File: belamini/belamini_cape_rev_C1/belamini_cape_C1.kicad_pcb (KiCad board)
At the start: 4 copper layers, 55 x 35 mm, 60 parts, among them IC1 TSV524xIQ4T, IC2 TSV524xIQ4T, IC3 ADS8168, IC4 TLV320AIC3104, IC5 MIC5317, IC6 USBLC6-2SC6, J1 Conn_01x10, J2 Conn_01x03, J3 Conn_01x03, J4 Conn_01x03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

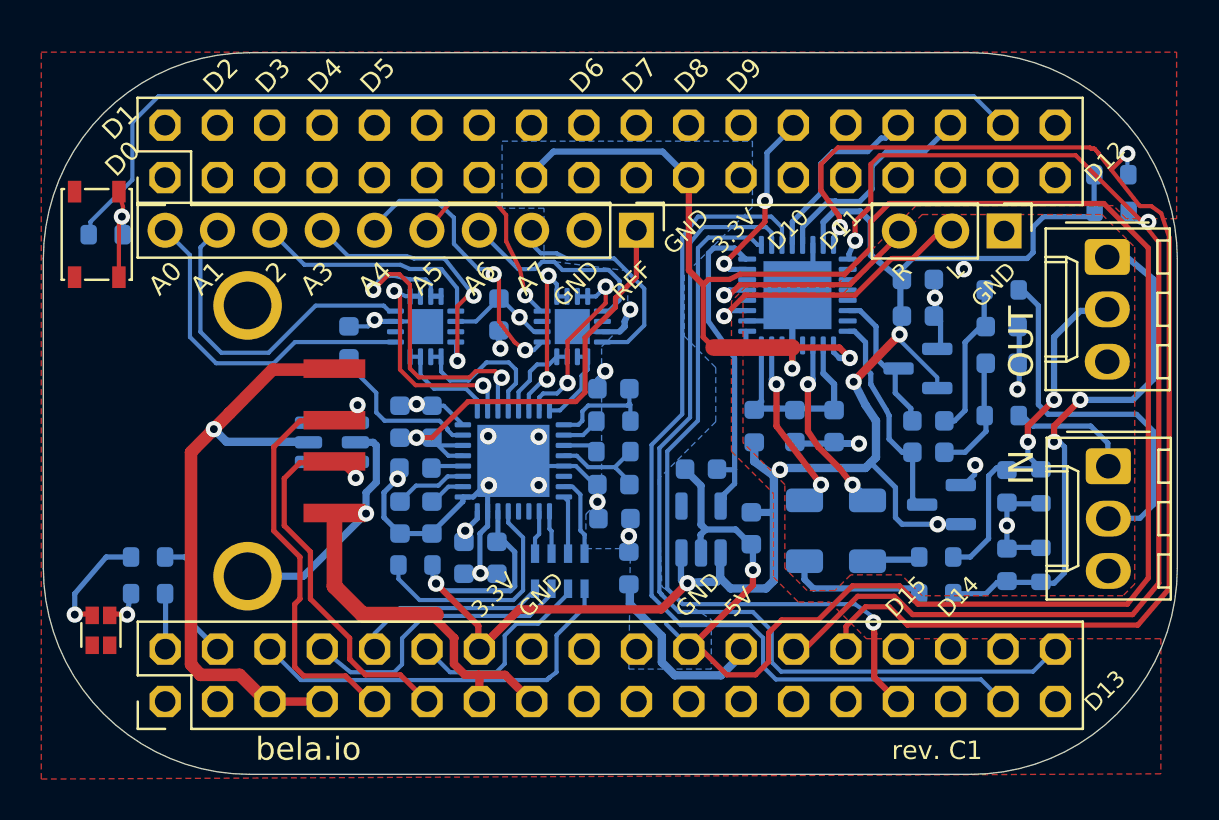
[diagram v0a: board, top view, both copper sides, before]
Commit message: Add logo to Mini rev. C1, clean up schematic and add production files
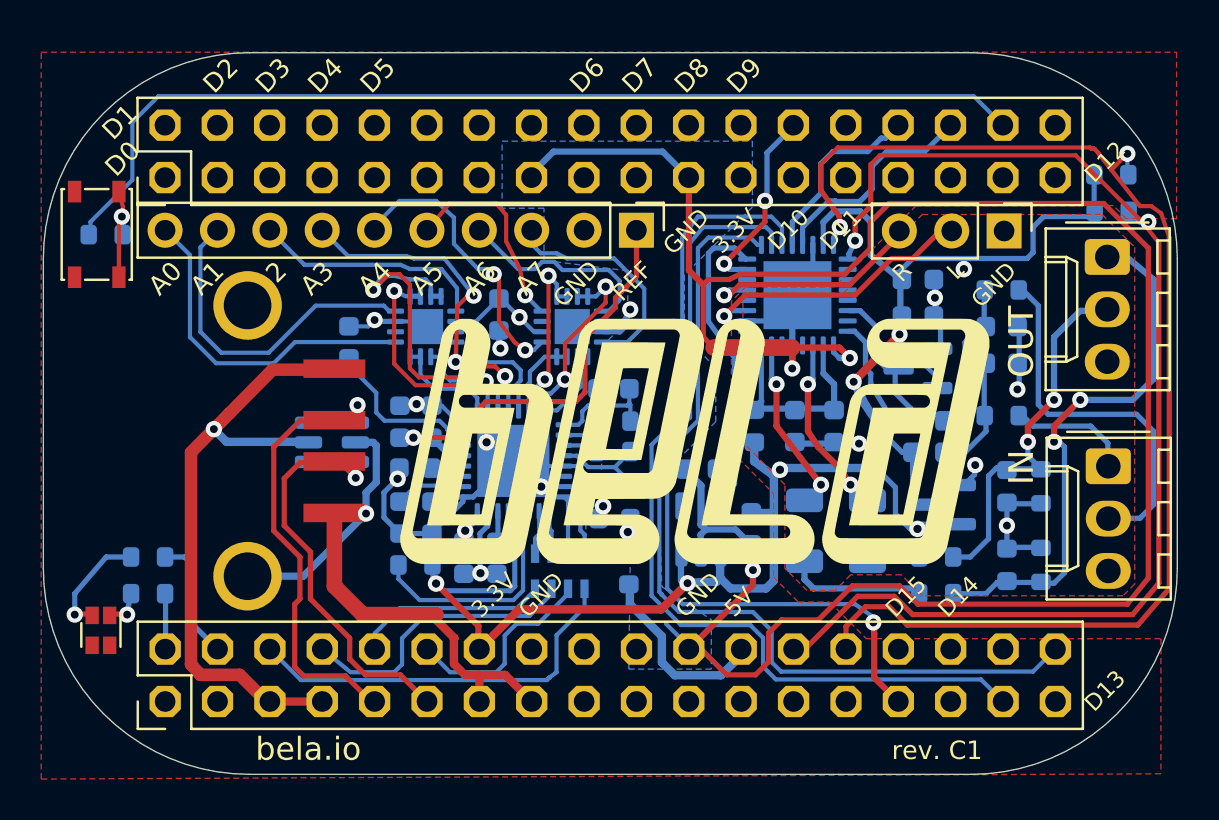
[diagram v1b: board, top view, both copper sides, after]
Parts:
- added G***: LOGO, Bela:bela_logo, F.Cu at (152.6, 106.3)
- D1, D2: value ESD -> PESD0603-240
- D5: value LED_Dual_AAKK -> LTST-C195TBJRKT
- FB1, FB2: value FerriteBead -> MPZ1608S121ATAH0
- S1: value SW_Push -> PTS810
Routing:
- net Net-(IC1-Pad13): track 10.9 -> 11.5 mm
- net GND: track 174.2 -> 174.3 mm, vias 20 -> 18
